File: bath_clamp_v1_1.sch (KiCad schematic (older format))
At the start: 56 parts, among them J1 105-1103-001, J2 105-1103-001, J3 105-1103-001, K1 1462042-8, K2 1462042-8, Q1 MBT3904DW1T1G, Q3 MBT3904DW1T1G, Q4 MBT3904DW1T1G, U1 OPA828, U11 AD8615, U12 TCA9555DBR, U14 OPA828, U15 TCA9554DW, U2 ADG1208, U3 G6L-1F-TR-DC5, U4 G6L-1F-TR-DC5, U5 G6L-1F-TR-DC5, U8 AD8615

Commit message: offset adjust to feedback buffer
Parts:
- removed C6: 5n, Capacitor_SMD:C_0603_1608Metric, symbol Device:C
- removed R31, R32, R33, R34: 10k, Resistor_SMD:R_0603_1608Metric, symbol Device:R_US
- removed U14: OPA828, Package_SO:SOIC-8_3.9x4.9mm_P1.27mm, symbol covg-kicad:OPA828
- added C?: 4.7n, Capacitor_SMD:C_0603_1608Metric, symbol Device:C
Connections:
- wire segments 287 -> 276
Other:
- note added: "Addr = 0111_A2_A1_A0"
- moved on the sheet: R8

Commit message: reduced ERC to just 4 warnings
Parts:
- removed U15: TCA9554DW, Package_SO:SOIC-16W_7.5x10.3mm_P1.27mm, symbol Interface_Expansion:TCA9554DW
- added U13: TCA9555DBR, Package_SO:SSOP-24_5.3x8.2mm_P0.65mm, symbol Interface_Expansion:TCA9555DBR
- gave numbers to parts that had none: 1
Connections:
- net labels added: CCOMP[1..4], RF1, RF2, RF3, RF4, RF[1..4]
- net labels removed: CCOMP[1:4], P1_CAL_SIG, P2_CAL_SIG
- wire segments 276 -> 285
- no-connect marks 5 -> 11
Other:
- note added: "TODO: what to do here?"
- note removed: "Addr = 0111_A2_A1_A0"
- moved on the sheet: U12

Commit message: updates to pcb layout
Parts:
- U3: footprint G6L-1F-TR-DC5_OMR -> covg-kicad:G6L-1F-TR-DC5
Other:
- note added: "0.2” long\nstandard is 0.4” long, check"
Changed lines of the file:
@@
 F 0 "U3" V 9997 4228 60  0000 L CNN
 F 1 "G6L-1F-TR-DC5" H 9700 4450 60  0000 L CNN
-F 2 "G6L-1F-TR-DC5_OMR" H 10250 4240 60  0001 C CNN
+F 2 "covg-kicad:G6L-1F-TR-DC5" H 10250 4240 60  0001 C CNN
 F 3 "" H 9450 4000 60  0000 C CNN
 F 4 "G6L-1F-TR-DC5" H 9997 4328 50  0001 C CNN "Manf#"
@@
 Wire Bus Line
 	9150 9050 9150 9500
+Text Notes 13350 3350 0    50   ~ 0
+0.2” long\nstandard is 0.4” long, check
 $EndSCHEMATC

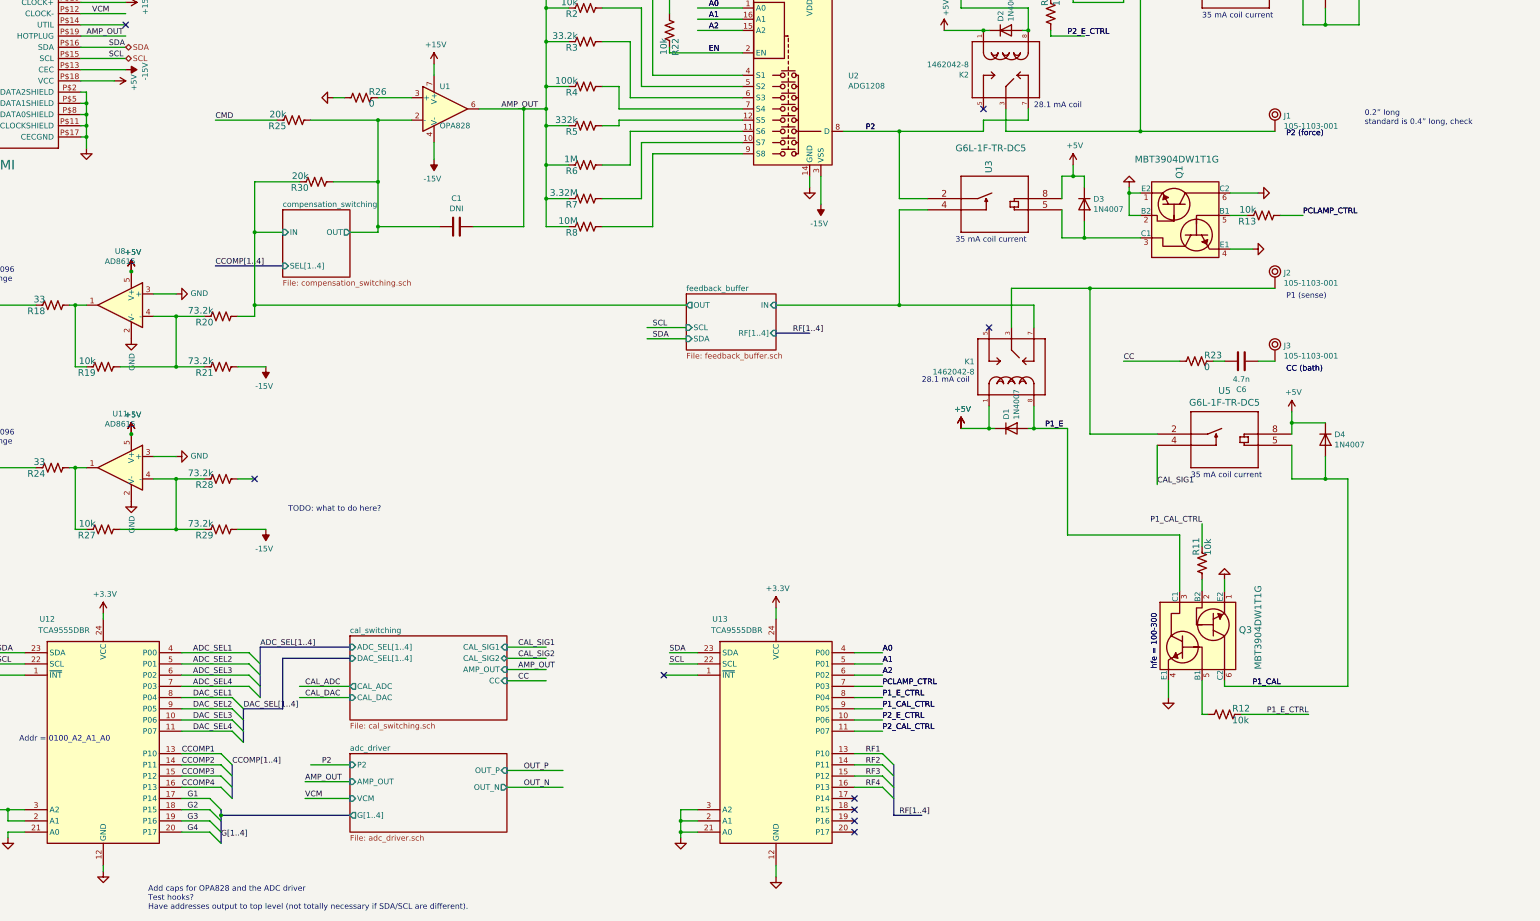
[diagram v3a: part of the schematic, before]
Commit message: added switching (partially) for current clamp
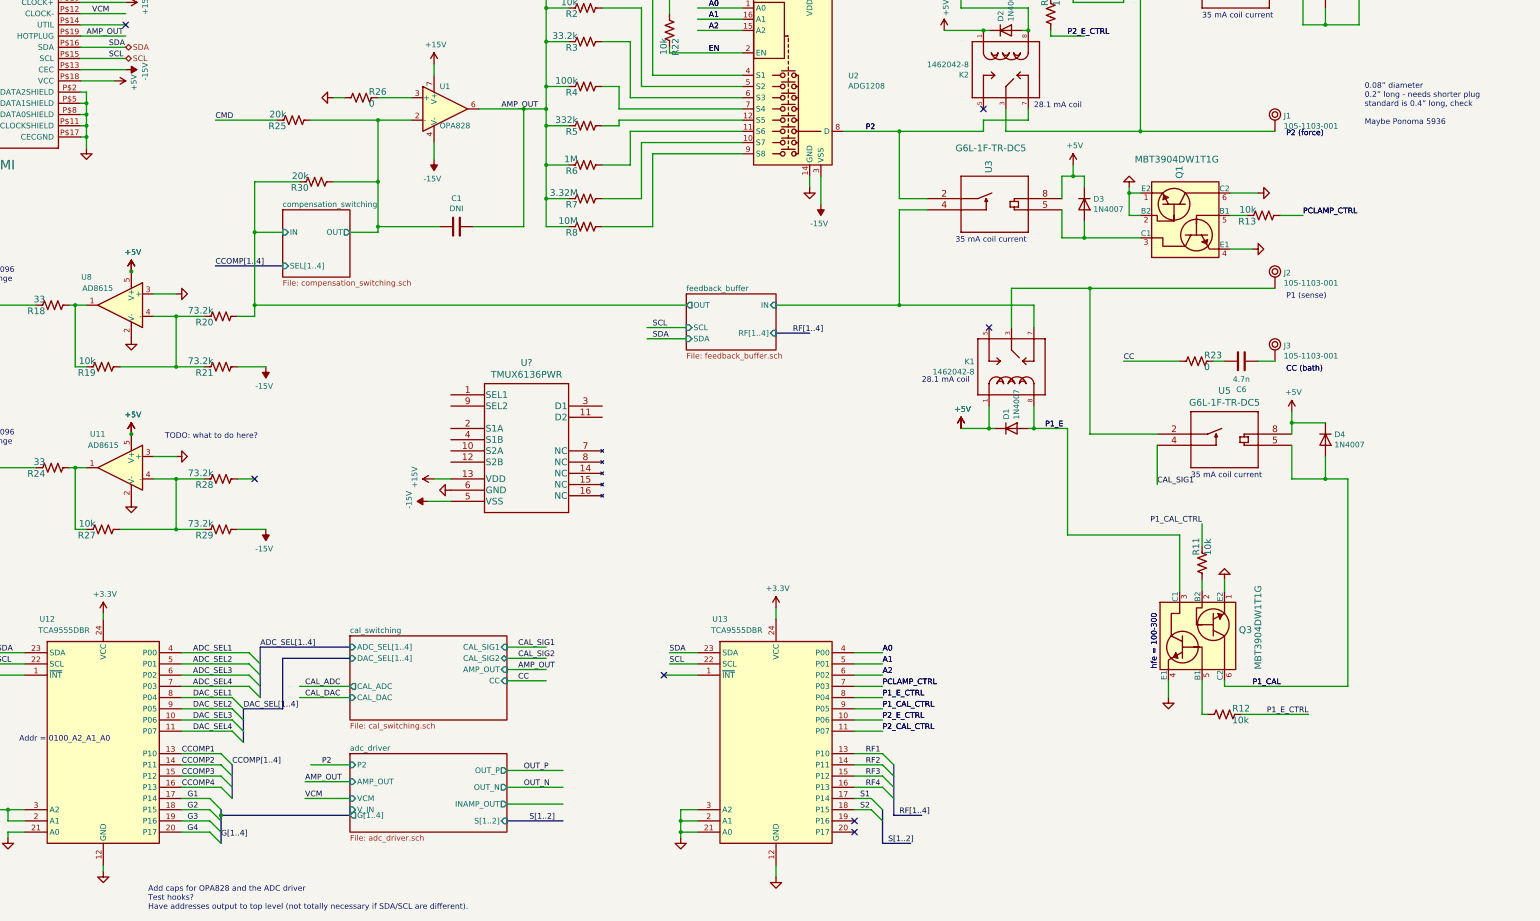
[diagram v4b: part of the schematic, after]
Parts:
- added U?: TMUX6136PWR, PW16_TEX, symbol covg-kicad:TMUX6136PWR
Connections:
- net labels added: S1, S2, S[1..2]
- wire segments 285 -> 290
- no-connect marks 11 -> 9
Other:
- note added: "0.08” diameter\n0.2” long - needs shorter plug\nstandard is 0.4” long, check\n\nMaybe Ponoma 5936"
- note removed: "0.2” long\nstandard is 0.4” long, check"
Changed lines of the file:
@@
 $EndDescr
-$Sheet
-S 4300 8950 1400 700
-U 608FDC40
-F0 "adc_driver" 50
-F1 "adc_driver.sch" 50
-F2 "P2" I L 4300 9050 50
-F3 "AMP_OUT" I L 4300 9200 50
-F4 "G[1..4]" O L 4300 9500 50
-F5 "VCM" I L 4300 9350 50
-F6 "OUT_P" I R 5700 9100 50
-F7 "OUT_N" O R 5700 9250 50
-$EndSheet
 $Sheet
 S 4300 7900 1400 750
@@
 P 2350 5250
 F 0 "#PWR0123" H 2350 5000 50  0001 C CNN
-F 1 "GND" V 2355 5122 50  0000 R CNN
+F 1 "GND" V 2355 5122 50  0001 R CNN
 F 2 "" H 2350 5250 50  0001 C CNN
 F 3 "" H 2350 5250 50  0001 C CNN
@@
 P 2750 4850
 F 0 "#PWR0120" H 2750 4600 50  0001 C CNN
-F 1 "GND" V 2755 4722 50  0000 R CNN
+F 1 "GND" V 2755 4722 50  0001 R CNN
 F 2 "" H 2750 4850 50  0001 C CNN
 F 3 "" H 2750 4850 50  0001 C CNN
@@
 U 1 1 6073E800
 P 2250 4950
-F 0 "U8" H 2250 5431 50  0000 C CNN
-F 1 "AD8615" H 2250 5340 50  0000 C CNN
+F 0 "U8" H 2550 5200 50  0000 C CNN
+F 1 "AD8615" H 2450 5100 50  0000 C CNN
 F 2 "Package_TO_SOT_SMD:TSOT-23-5" H 2250 4950 50  0001 C CNN
 F 3 "https://www.analog.com/media/en/technical-documentation/data-sheets/AD8615_8616_8618.pdf" H 2250 5150 50  0001 C CNN
@@
 P 2350 6700
 F 0 "#PWR020" H 2350 6450 50  0001 C CNN
-F 1 "GND" V 2355 6572 50  0000 R CNN
+F 1 "GND" V 2355 6572 50  0001 R CNN
 F 2 "" H 2350 6700 50  0001 C CNN
 F 3 "" H 2350 6700 50  0001 C CNN
@@
 P 2750 6300
 F 0 "#PWR021" H 2750 6050 50  0001 C CNN
-F 1 "GND" V 2755 6172 50  0000 R CNN
+F 1 "GND" V 2755 6172 50  0001 R CNN
 F 2 "" H 2750 6300 50  0001 C CNN
 F 3 "" H 2750 6300 50  0001 C CNN
@@
 U 1 1 60AFE6BC
 P 2250 6400
-F 0 "U11" H 2250 6881 50  0000 C CNN
-F 1 "AD8615" H 2250 6790 50  0000 C CNN
+F 0 "U11" H 2450 6700 50  0000 C CNN
+F 1 "AD8615" H 2400 6600 50  0000 C CNN
 F 2 "Package_TO_SOT_SMD:TSOT-23-5" H 2250 6400 50  0001 C CNN
 F 3 "https://www.analog.com/media/en/technical-documentation/data-sheets/AD8615_8616_8618.pdf" H 2250 6600 50  0001 C CNN
@@
 Text Label 9200 9500 0    50   ~ 0
 RF[1..4]
-NoConn ~ 8800 9350
-NoConn ~ 8800 9450
 NoConn ~ 8800 9550
 NoConn ~ 8800 9650
@@
 RF[1..4]
 NoConn ~ 3450 6500
-Text Notes 3750 6800 0    50   ~ 0
+Text Notes 2650 6150 0    50   ~ 0
 TODO: what to do here?
 NoConn ~ 850  6400
+Text Notes 13350 3350 0    50   ~ 0
+0.08” diameter\n0.2” long - needs shorter plug\nstandard is 0.4” long, check\n\nMaybe Ponoma 5936
+$Comp
+L covg-kicad:TMUX6136PWR U?
+U 1 1 60A974B3
+P 5200 5750
+F 0 "U?" H 5875 6037 60  0000 C CNN
+F 1 "TMUX6136PWR" H 5875 5931 60  0000 C CNN
+F 2 "PW16_TEX" H 5850 5850 60  0001 C CNN
+F 3 "" H 5200 5750 60  0000 C CNN
+	1    5200 5750
+	1    0    0    -1
+$EndComp
+$Comp
+L power:-15V #PWR?
+U 1 1 60A994AC
+P 5000 6700
+F 0 "#PWR?" H 5000 6800 50  0001 C CNN
+F 1 "-15V" H 5015 6873 50  0000 C CNN
+F 2 "" H 5000 6700 50  0001 C CNN
+F 3 "" H 5000 6700 50  0001 C CNN
+	1    5000 6700
+	0    -1   -1   0
+$EndComp
+$Comp
+L power:GND #PWR?
+U 1 1 60A99C58
+P 5200 6600
+F 0 "#PWR?" H 5200 6350 50  0001 C CNN
+F 1 "GND" V 5205 6472 50  0001 R CNN
+F 2 "" H 5200 6600 50  0001 C CNN
+F 3 "" H 5200 6600 50  0001 C CNN
+	1    5200 6600
+	0    1    1    0
+$EndComp
+Wire Wire Line
+	5000 6700 5200 6700
+$Comp
+L power:+15V #PWR?
+U 1 1 60AB61A5
+P 5050 6500
+F 0 "#PWR?" H 5050 6350 50  0001 C CNN
+F 1 "+15V" H 5065 6673 50  0000 C CNN
+F 2 "" H 5050 6500 50  0001 C CNN
+F 3 "" H 5050 6500 50  0001 C CNN
+	1    5050 6500
+	0    -1   -1   0
+$EndComp
+Wire Wire Line
+	5050 6500 5200 6500
+$Sheet
+S 4300 8950 1400 700
+U 608FDC40
+F0 "adc_driver" 50
+F1 "adc_driver.sch" 50
+F2 "P2" I L 4300 9050 50
+F3 "AMP_OUT" I L 4300 9200 50
+F4 "G[1..4]" O L 4300 9500 50
+F5 "VCM" I L 4300 9350 50
+F6 "OUT_N" O R 5700 9250 50
+F7 "INAMP_OUT" O R 5700 9400 50
+F8 "V_IN" I L 4300 9450 50
+F9 "S[1..2]" I R 5700 9550 50
+F10 "OUT_P" O R 5700 9100 50
+$EndSheet
+Wire Wire Line
+	5700 9400 6200 9400
+Wire Wire Line
+	8800 9450 8950 9450
+Wire Wire Line
+	8800 9350 8950 9350
+Text Label 8850 9350 0    50   ~ 0
+S1
+Text Label 8850 9450 0    50   ~ 0
+S2
+Entry Wire Line
+	8950 9350 9050 9450
+Entry Wire Line
+	8950 9450 9050 9550
+Wire Bus Line
+	9050 9750 9300 9750
+Text Label 9100 9750 0    50   ~ 0
+S[1..2]
+Wire Bus Line
+	5700 9550 6200 9550
+Wire Bus Line
+	9050 9450 9050 9750
 Wire Bus Line
 	3250 9050 3250 9350
@@
 	3350 8550 3350 8850
 Wire Bus Line
+	9150 9050 9150 9500
+Wire Bus Line
 	3500 8000 3500 8450
-Wire Bus Line
-	9150 9050 9150 9500
-Text Notes 13350 3350 0    50   ~ 0
-0.2” long\nstandard is 0.4” long, check
+Text Label 5900 9550 0    50   ~ 0
+S[1..2]
 $EndSCHEMATC

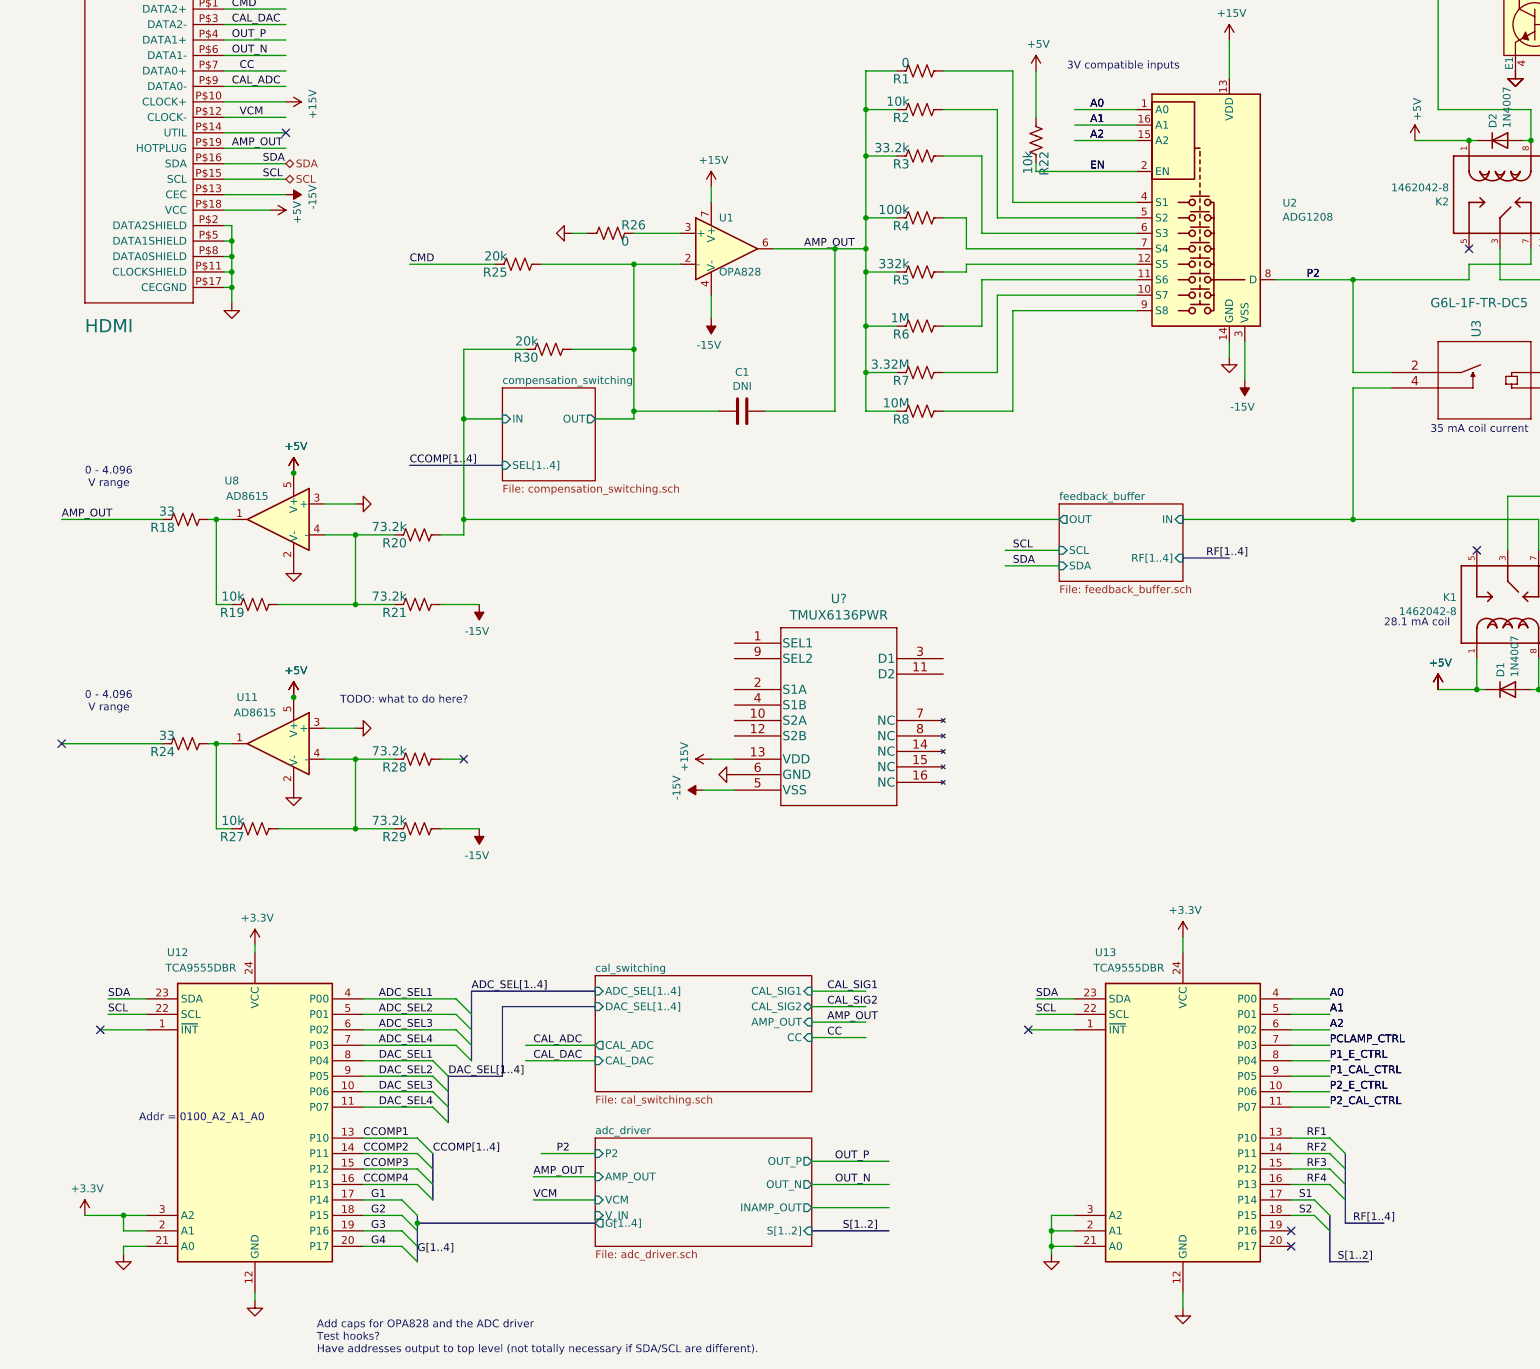
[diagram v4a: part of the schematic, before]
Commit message: before adding Howland for current clamp
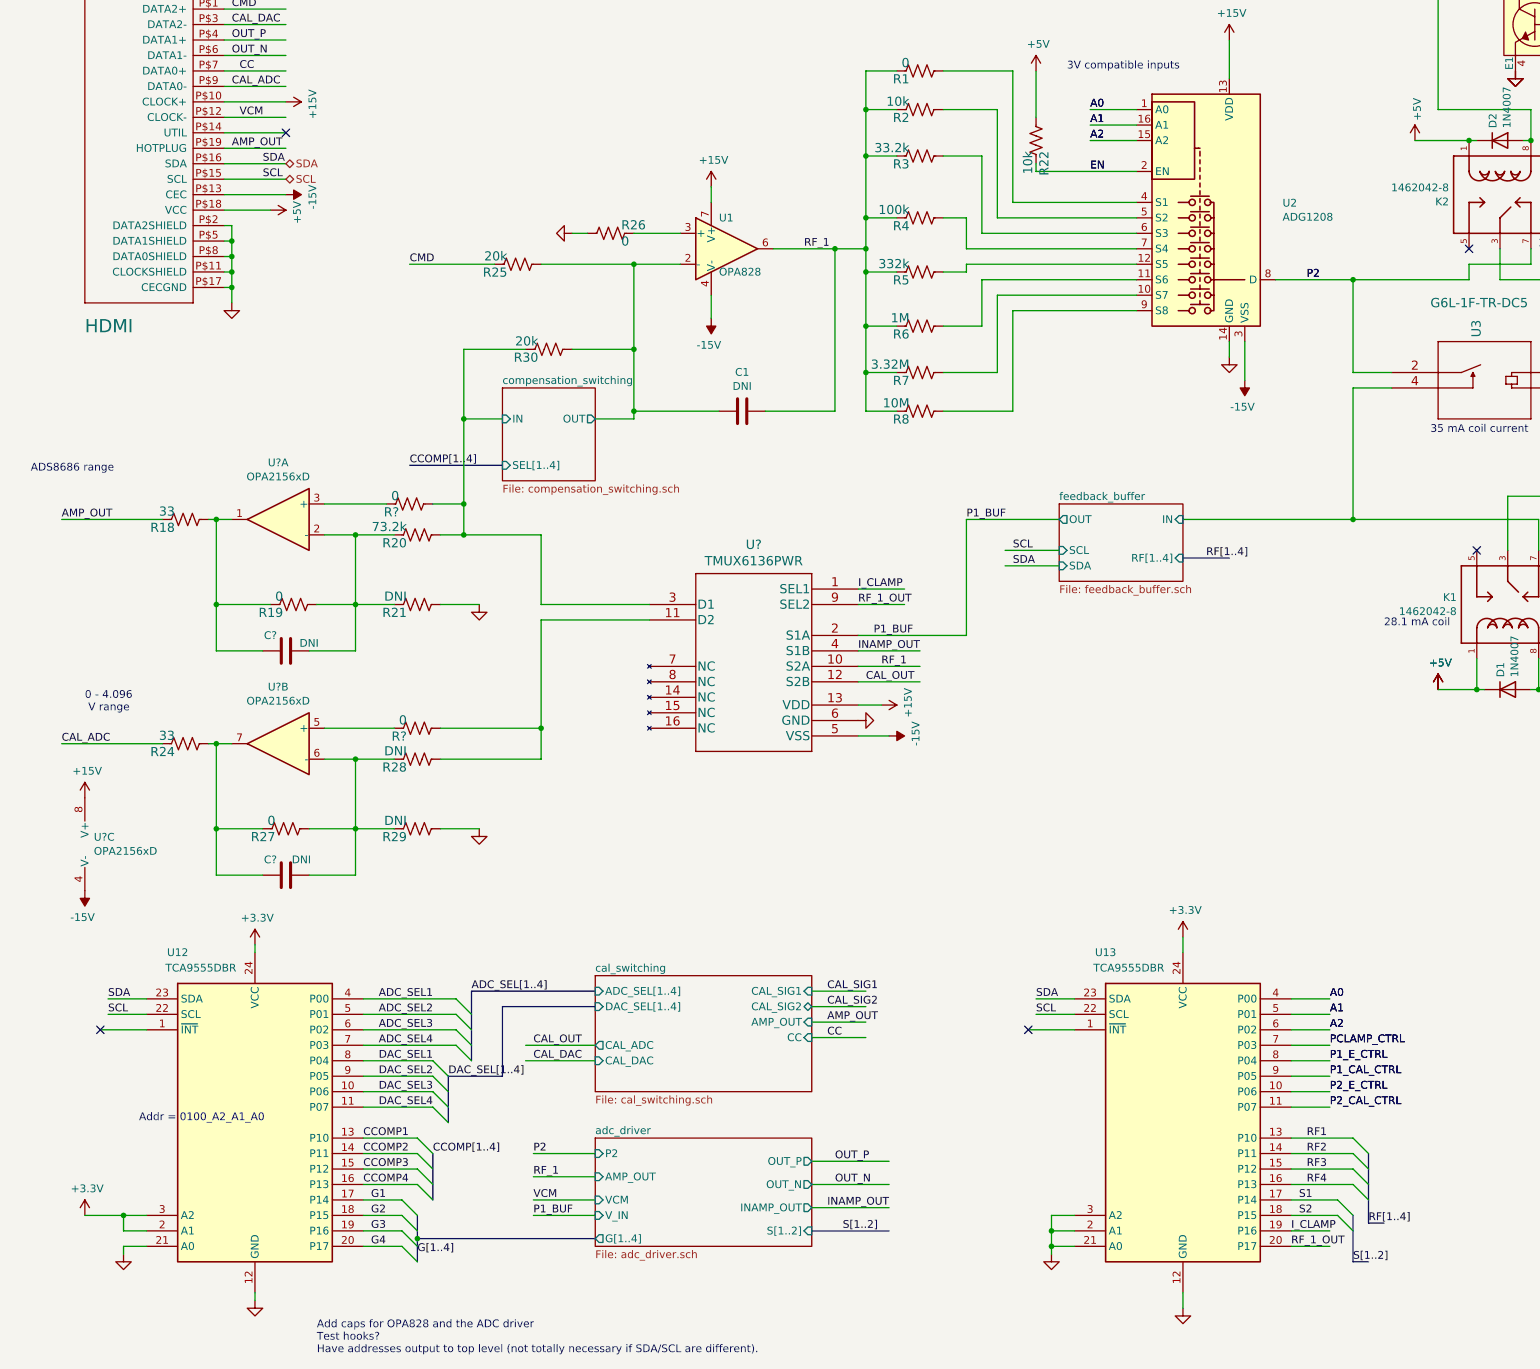
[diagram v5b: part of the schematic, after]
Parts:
- removed U11, U8: AD8615, Package_TO_SOT_SMD:TSOT-23-5, symbol covg-kicad:AD8615
- added C? (x2): DNI, Capacitor_SMD:C_0603_1608Metric, symbol Device:C
- added R? (x2): 0, Resistor_SMD:R_0603_1608Metric, symbol Device:R_US
- added U? (x3): OPA2156xD, Package_SO:SOIC-8_3.9x4.9mm_P1.27mm, symbol Amplifier_Operational:OPA2156xD
- R19, R27: value 10k -> 0; Manf# RC0603FR-0710KL -> RC0603FR-070RL
- R21, R28, R29: value 73.2k -> DNI
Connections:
- net labels added: CAL_OUT, INAMP_OUT, I_CLAMP, P1_BUF, RF_1, RF_1_OUT
- wire segments 290 -> 316
- no-connect marks 9 -> 5
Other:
- note added: "ADS8686 range\n +/-2.5V, +/-5V, +/-10V"
- note removed: "TODO: what to do here?"
- moved on the sheet: R19, R27, U?
